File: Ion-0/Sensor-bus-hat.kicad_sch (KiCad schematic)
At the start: 96 parts, among them J10 Conn_CAN, J11 Conn_Prob_1, J12 Conn_Prob_2, J13 Conn_01x04, J15 Conn_01x04, J6 Coaxial_Small, J8 Conn_Heater, J9 Conn_prob_3, Q2 IRLML6244, U1 HDC2080, U2 MS5607-02BA, U3 BNO085, U4 TCA9617ADGKR, U5 A4988SETTR-T, U6 MAX-M10M-00B, U7 TPS3850H50DRCR, U8 SN65HVD230, Y2 9HT10-32.768KBZF-T

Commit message: BUZZER NEVER DIES
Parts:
- added BZ1: Buzzer, Buzzer_Beeper:Buzzer_CUI_CPT-9019S-SMT, symbol Device:Buzzer
- added Q1: IRLML6244, Package_TO_SOT_SMD:SOT-23, symbol Transistor_FET:IRLML6244
- added R45, R46: 330, Resistor_SMD:R_0603_1608Metric_Pad0.98x0.95mm_HandSolder, symbol Device:R_Small_US
- C25, C26, C27, C28, C29: footprint (none) -> Capacitor_SMD:C_0603_1608Metric
- J15: footprint (none) -> TerminalBlock:TerminalBlock_MaiXu_MX126-5.0-04P_1x04_P5.00mm
- R19, R20, R21, R22, R43, R44: footprint (none) -> Resistor_SMD:R_0603_1608Metric_Pad0.98x0.95mm_HandSolder
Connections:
- net +5V: now also BZ1.1 (+), R45.1
- net GND: now also Q1.2 (S)
- new net: Q1.1 (G), R46.2
- new net: BZ1.2 (-), Q1.3 (D), R45.2
- new net Buzzer: R46.1

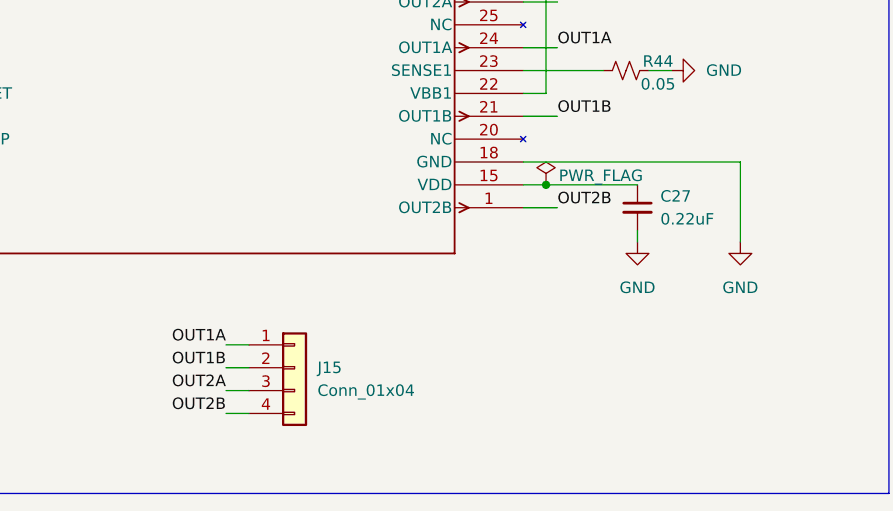
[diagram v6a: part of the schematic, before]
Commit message: version 0.8 - stepper driver included and better detailled schematic
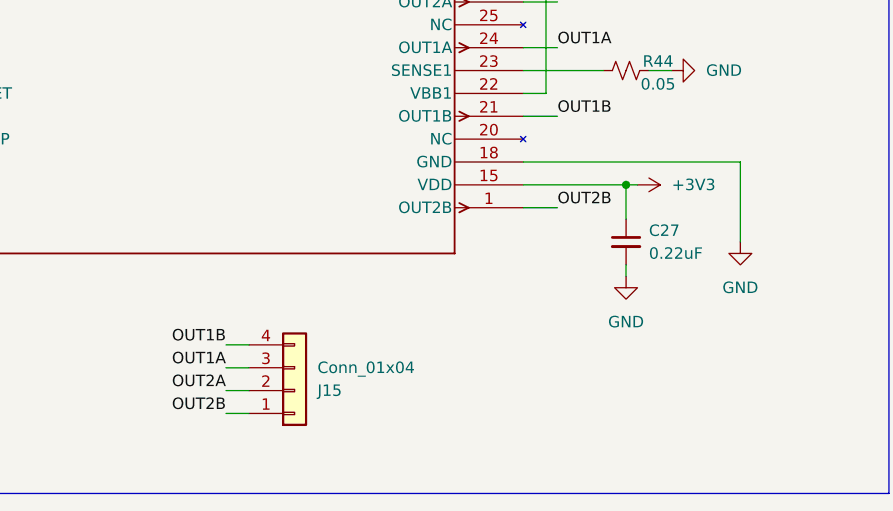
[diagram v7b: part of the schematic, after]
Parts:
- J15: footprint TerminalBlock:TerminalBlock_MaiXu_MX126-5.0-04P_1x04_P5.00mm -> TerminalBlock:TerminalBlock_Xinya_XY308-2.54-4P_1x04_P2.54mm_Horizontal
- U5: footprint QFN-28_ALM -> 1_Ion:QFN-28_ALM
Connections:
- net +3V3: now also C27.1, U5.15 (VDD)
- net OUT1A: now also J15.3 (Pin_3); no longer J15.1 (Pin_1)
- net OUT1B: now also J15.4 (Pin_4); no longer J15.2 (Pin_2)
- net OUT2A: now also J15.2 (Pin_2); no longer J15.3 (Pin_3)
- net OUT2B: now also J15.1 (Pin_1); no longer J15.4 (Pin_4)
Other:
- moved on the sheet: C27
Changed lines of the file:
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@@
 	)
 	(junction
-		(at 130.81 247.65)
+		(at 139.7 247.65)
 		(diameter 0)
 		(color 0 0 0 0)
@@
 	(wire
 		(pts
+			(xy 139.7 251.46) (xy 139.7 247.65)
+		)
+		(stroke
+			(width 0)
+			(type default)
+		)
+	)
+	(wire
+		(pts
 			(xy 170.18 45.72) (xy 170.18 55.88)
 		)
@@
 	(wire
 		(pts
+			(xy 139.7 247.65) (xy 140.97 247.65)
+		)
+		(stroke
+			(width 0)
+			(type default)
+		)
+	)
+	(wire
+		(pts
 			(xy 322.58 33.02) (xy 337.82 33.02)
 		)
@@
 	(wire
 		(pts
-			(xy 140.97 252.73) (xy 140.97 254)
+			(xy 139.7 256.54) (xy 139.7 257.81)
 		)
 		(stroke
@@
 	(wire
 		(pts
+			(xy 139.7 247.65) (xy 128.27 247.65)
+		)
+		(stroke
+			(width 0)
+			(type default)
+		)
+	)
+	(wire
+		(pts
 			(xy 149.86 175.26) (xy 152.4 175.26)
 		)
@@
 	(wire
 		(pts
-			(xy 128.27 247.65) (xy 130.81 247.65)
-		)
-		(stroke
-			(width 0)
-			(type default)
-		)
-	)
-	(wire
-		(pts
 			(xy 279.4 97.79) (xy 283.21 97.79)
 		)
@@
 	(wire
 		(pts
-			(xy 130.81 247.65) (xy 140.97 247.65)
-		)
-		(stroke
-			(width 0)
-			(type default)
-		)
-	)
-	(wire
-		(pts
 			(xy 191.77 167.64) (xy 191.77 179.07)
 		)
@@
 	)
 	(label "OUT1B"
-		(at 95.25 267.97 180)
+		(at 95.25 265.43 180)
 		(effects
 			(font
@@
 	)
 	(label "OUT1A"
-		(at 95.25 265.43 180)
+		(at 95.25 267.97 180)
 		(effects
 			(font
@@
 	(symbol
 		(lib_id "power:GND")
-		(at 140.97 254 0)
+		(at 139.7 257.81 0)
 		(unit 1)
 		(body_style 1)
@@
 		(fields_autoplaced yes)
 		(property "Reference" "#PWR0101"
-			(at 140.97 260.35 0)
+			(at 139.7 264.16 0)
 			(hide yes)
 			(show_name no)
@@
 		)
 		(property "Value" "GND"
-			(at 140.97 259.08 0)
+			(at 139.7 262.89 0)
 			(show_name no)
 			(do_not_autoplace no)
@@
 		)
 		(property "Footprint" ""
-			(at 140.97 254 0)
+			(at 139.7 257.81 0)
 			(hide yes)
 			(show_name no)
@@
 		)
 		(property "Datasheet" ""
-			(at 140.97 254 0)
+			(at 139.7 257.81 0)
 			(hide yes)
 			(show_name no)
@@
 		)
 		(property "Description" "Power symbol creates a global label with name \"GND\" , ground"
-			(at 140.97 254 0)
+			(at 139.7 257.81 0)
 			(hide yes)
 			(show_name no)
@@
 	(symbol
 		(lib_id "Connector_Generic:Conn_01x04")
-		(at 102.87 267.97 0)
+		(at 102.87 270.51 0)
+		(mirror x)
 		(unit 1)
 		(body_style 1)
@@
 		(in_pos_files yes)
 		(dnp no)
-		(fields_autoplaced yes)
 		(property "Reference" "J15"
-			(at 105.41 267.9699 0)
+			(at 105.41 270.5101 0)
 			(show_name no)
 			(do_not_autoplace no)
@@
 		)
 		(property "Value" "Conn_01x04"
-			(at 105.41 270.5099 0)
+			(at 105.41 267.9701 0)
 			(show_name no)
 			(do_not_autoplace no)
@@
 			)
 		)
-		(property "Footprint" "TerminalBlock:TerminalBlock_MaiXu_MX126-5.0-04P_1x04_P5.00mm"
-			(at 102.87 267.97 0)
+		(property "Footprint" "TerminalBlock:TerminalBlock_Xinya_XY308-2.54-4P_1x04_P2.54mm_Horizontal"
+			(at 102.87 270.51 0)
 			(hide yes)
 			(show_name no)
@@
 		)
 		(property "Datasheet" ""
-			(at 102.87 267.97 0)
+			(at 102.87 270.51 0)
 			(hide yes)
 			(show_name no)
@@
 		)
 		(property "Description" "Generic connector, single row, 01x04, script generated (kicad-library-utils/schlib/autogen/connector/)"
-			(at 102.87 267.97 0)
+			(at 102.87 270.51 0)
 			(hide yes)
 			(show_name no)
@@
 	(symbol
 		(lib_id "Device:C_Small")
-		(at 140.97 250.19 0)
+		(at 139.7 254 0)
 		(unit 1)
 		(body_style 1)
@@
 		(fields_autoplaced yes)
 		(property "Reference" "C27"
-			(at 143.51 248.9262 0)
+			(at 142.24 252.7362 0)
 			(show_name no)
 			(do_not_autoplace no)
@@
 		)
 		(property "Value" "0.22uF"
-			(at 143.51 251.4662 0)
+			(at 142.24 255.2762 0)
 			(show_name no)
 			(do_not_autoplace no)
@@
 		)
 		(property "Footprint" "Capacitor_SMD:C_0603_1608Metric"
-			(at 140.97 250.19 0)
+			(at 139.7 254 0)
 			(hide yes)
 			(show_name no)
@@
 		)
 		(property "Datasheet" ""
-			(at 140.97 250.19 0)
+			(at 139.7 254 0)
 			(hide yes)
 			(show_name no)
@@
 		)
 		(property "Description" "Unpolarized capacitor, small symbol"
-			(at 140.97 250.19 0)
+			(at 139.7 254 0)
 			(hide yes)
 			(show_name no)
@@
 			)
 		)
-		(property "Footprint" "QFN-28_ALM"
+		(property "Footprint" "1_Ion:QFN-28_ALM"
 			(at 57.15 212.09 0)
 			(hide yes)
@@
 	)
 	(symbol
-		(lib_id "power:PWR_FLAG")
-		(at 130.81 247.65 0)
-		(unit 1)
-		(body_style 1)
-		(exclude_from_sim no)
-		(in_bom yes)
-		(on_board yes)
-		(in_pos_files yes)
-		(dnp no)
-		(property "Reference" "#FLG07"
-			(at 130.81 245.745 0)
-			(hide yes)
-			(show_name no)
-			(do_not_autoplace no)
-			(effects
-				(font
-					(size 1.27 1.27)
-				)
-			)
-		)
-		(property "Value" "PWR_FLAG"
-			(at 136.906 246.634 0)
-			(show_name no)
-			(do_not_autoplace no)
-			(effects
-				(font
-					(size 1.27 1.27)
-				)
-			)
-		)
-		(property "Footprint" ""
-			(at 130.81 247.65 0)
-			(hide yes)
-			(show_name no)
-			(do_not_autoplace no)
-			(effects
-				(font
-					(size 1.27 1.27)
-				)
-			)
-		)
-		(property "Datasheet" ""
-			(at 130.81 247.65 0)
-			(hide yes)
-			(show_name no)
-			(do_not_autoplace no)
-			(effects
-				(font
-					(size 1.27 1.27)
-				)
-			)
-		)
-		(property "Description" "Special symbol for telling ERC where power comes from"
-			(at 130.81 247.65 0)
-			(hide yes)
-			(show_name no)
-			(do_not_autoplace no)
-			(effects
-				(font
-					(size 1.27 1.27)
-				)
-			)
-		)
-		(pin "1"
-		)
-		(instances
-			(project "Ion-0"
-				(path "/8323d88f-a402-4af7-9e3a-bb7cf2dffd76/9244a77a-082d-413f-981e-aeac06b4b15b"
-					(reference "#FLG07")
-					(unit 1)
-				)
-			)
-		)
-	)
-	(symbol
 		(lib_id "power:GND")
 		(at 274.32 166.37 0)
@@
 					(unit 1)
 				)
+			)
+		)
+	)
+	(symbol
+		(lib_id "power:+3V3")
+		(at 140.97 247.65 270)
+		(unit 1)
+		(body_style 1)
+		(exclude_from_sim no)
+		(in_bom yes)
+		(on_board yes)
+		(in_pos_files yes)
+		(dnp no)
+		(fields_autoplaced yes)
+		(property "Reference" "#PWR082"
+			(at 137.16 247.65 0)
+			(hide yes)
+			(show_name no)
+			(do_not_autoplace no)
+			(effects
+				(font
+					(size 1.27 1.27)
+				)
+			)
+		)
+		(property "Value" "+3V3"
+			(at 144.78 247.6499 90)
+			(show_name no)
+			(do_not_autoplace no)
+			(effects
+				(font
+					(size 1.27 1.27)
+				)
+				(justify left)
+			)
+		)
+		(property "Footprint" ""
+			(at 140.97 247.65 0)
+			(hide yes)
+			(show_name no)
+			(do_not_autoplace no)
+			(effects
+				(font
+					(size 1.27 1.27)
+				)
+			)
+		)
+		(property "Datasheet" ""
+			(at 140.97 247.65 0)
+			(hide yes)
+			(show_name no)
+			(do_not_autoplace no)
+			(effects
+				(font
+					(size 1.27 1.27)
+				)
+			)
+		)
+		(property "Description" "Power symbol creates a global label with name \"+3V3\""
+			(at 140.97 247.65 0)
+			(hide yes)
+			(show_name no)
+			(do_not_autoplace no)
+			(effects
+				(font
+					(size 1.27 1.27)
+				)
+			)
+		)
+		(pin "1"
+		)
+		(instances
+			(project "Ion-0"
+				(path "/8323d88f-a402-4af7-9e3a-bb7cf2dffd76/9244a77a-082d-413f-981e-aeac06b4b15b"
+					(reference "#PWR082")
+					(unit 1)
+				)

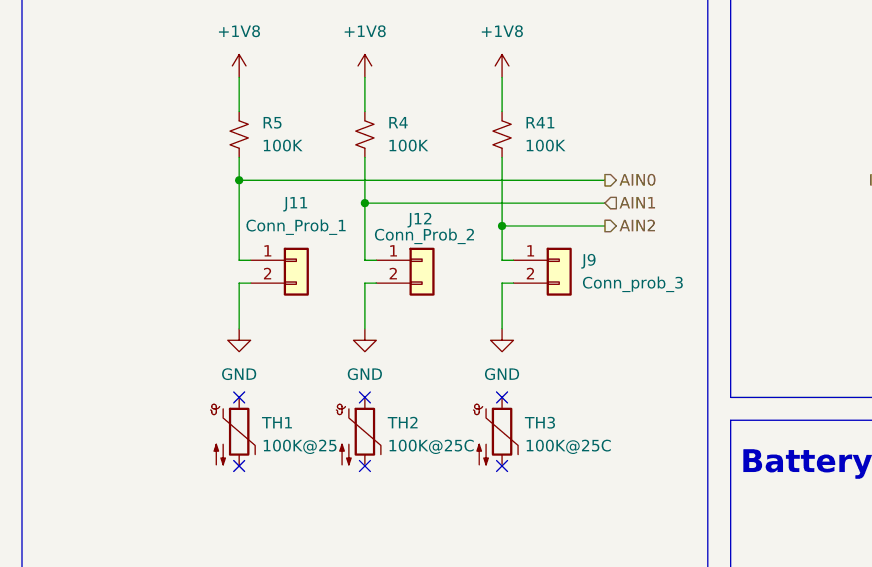
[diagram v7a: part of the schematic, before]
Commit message: connectors fixes
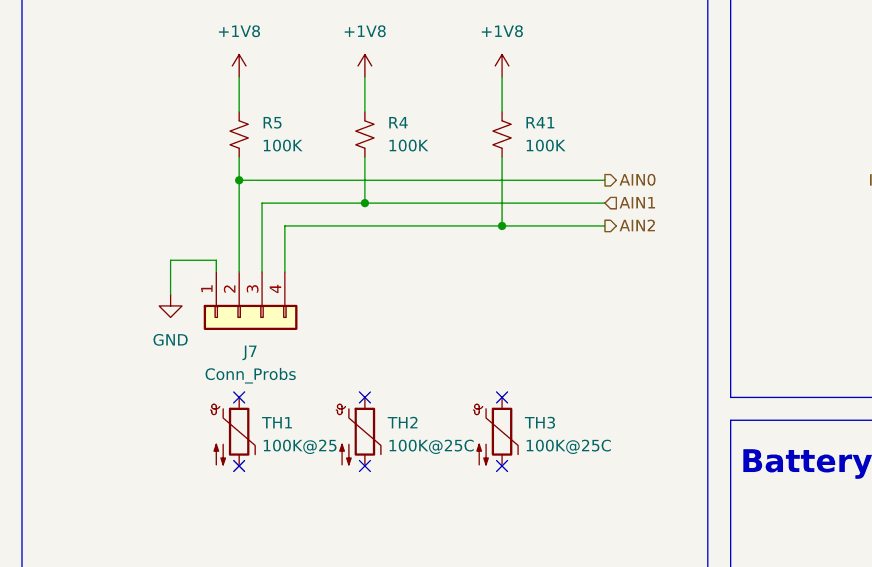
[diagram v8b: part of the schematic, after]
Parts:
- removed J11: Conn_Prob_1, TerminalBlock:TerminalBlock_Xinya_XY308-2.54-2P_1x02_P2.54mm_Horizontal, symbol Connector_Generic:Conn_01x02
- removed J12: Conn_Prob_2, TerminalBlock:TerminalBlock_Xinya_XY308-2.54-2P_1x02_P2.54mm_Horizontal, symbol Connector_Generic:Conn_01x02
- removed J9: Conn_prob_3, TerminalBlock:TerminalBlock_Xinya_XY308-2.54-2P_1x02_P2.54mm_Horizontal, symbol Connector_Generic:Conn_01x02
- added J7: Conn_Probs, Connector_JST:JST_XH_B4B-XH-AM_1x04_P2.50mm_Vertical, symbol Connector_Generic:Conn_01x04
- J15: footprint TerminalBlock:TerminalBlock_Xinya_XY308-2.54-4P_1x04_P2.54mm_Horizontal -> Connector_JST:JST_XH_B4B-XH-AM_1x04_P2.50mm_Vertical
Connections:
- net AIN0: now also J7.2 (Pin_2)
- net AIN1: now also J7.3 (Pin_3)
- net AIN2: now also J7.4 (Pin_4)
- net GND: now also J7.1 (Pin_1)
